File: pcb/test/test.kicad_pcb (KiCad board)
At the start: 2 copper layers, 27 parts, among them IC1 ADG904BRUZ-REEL7, J1 CONSMA013.062-G, J3 Conn_01x04, U2 TL081

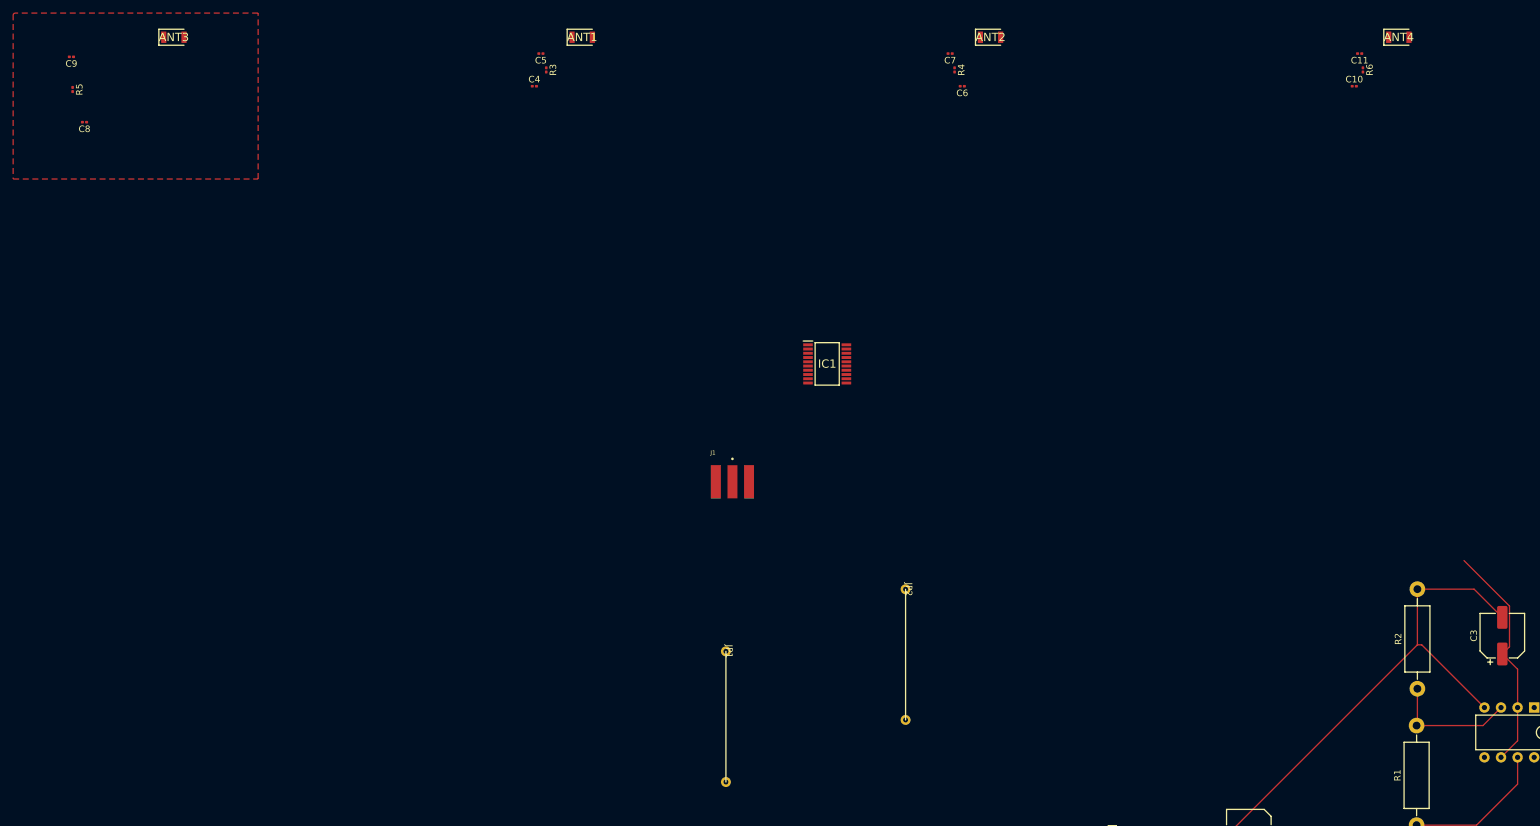
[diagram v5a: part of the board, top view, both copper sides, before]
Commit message: routage guides d'onde
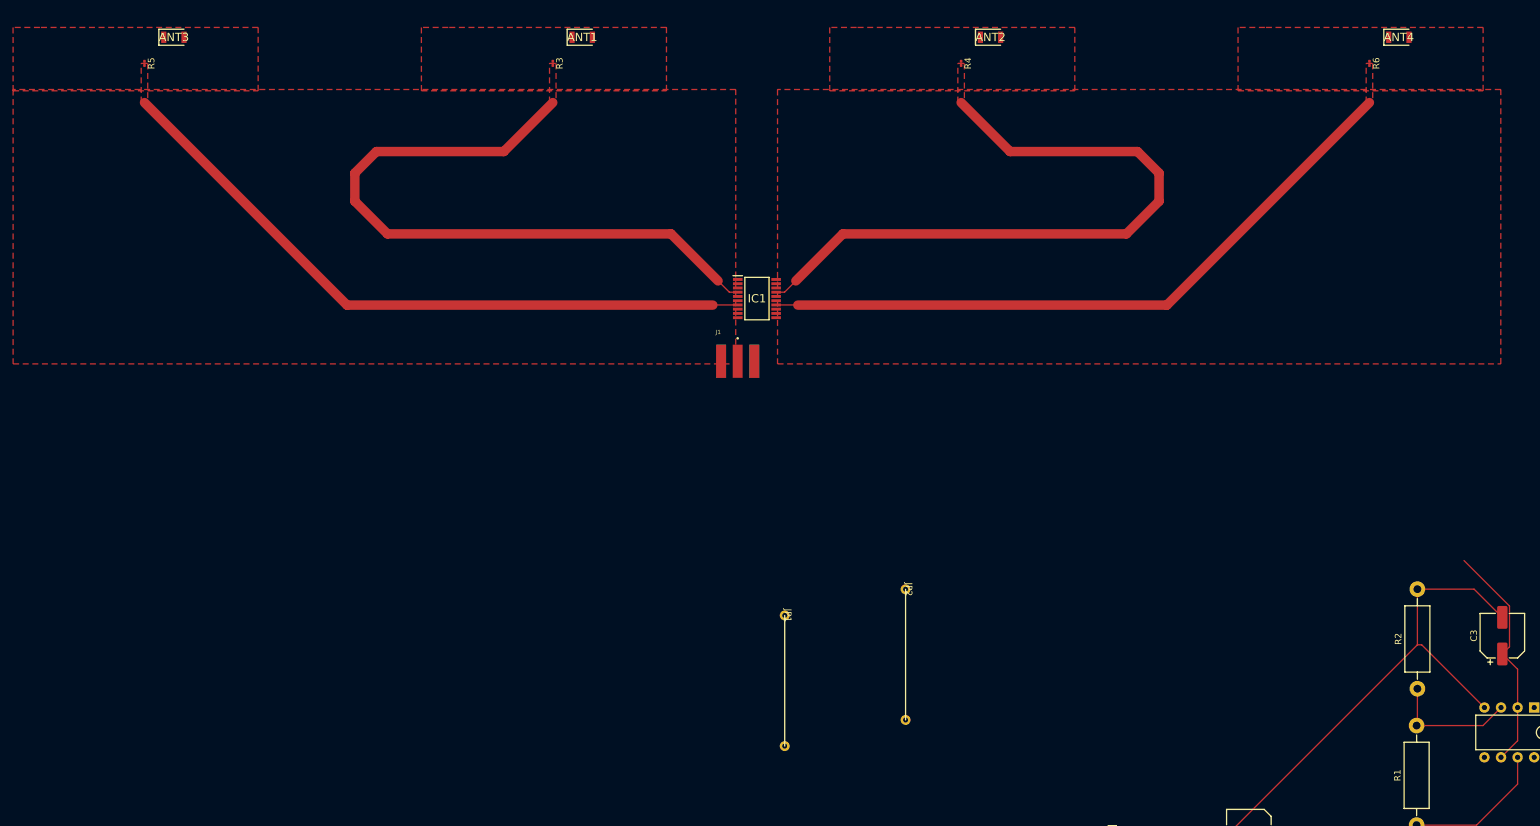
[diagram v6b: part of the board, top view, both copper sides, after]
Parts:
- removed C10, C11, C4, C5, C6, C7, C8, C9: C, Capacitor_SMD:C_0201_0603Metric
- moved J1 18.5 mm to (136.3, 102.1)
- moved IC1 14.7 mm to (139.2, 90.0)
- moved R5 11.7 mm to (45.5, 54.0)
- moved JP1 10.5 mm to (143.5, 138.5)
- moved R3 1.41 mm to (108.0, 54.0)
- moved R4 1.41 mm to (170.5, 54.0)
- moved R6 1.41 mm to (233.0, 54.0)
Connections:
- ANT1 pad 1: Net-(ANT1-FEED) -> GND
- ANT2 pad 1: Net-(ANT2-FEED) -> GND
- ANT3 pad 1: Net-(ANT3-FEED) -> GND
- ANT4 pad 1: Net-(ANT4-FEED) -> GND
- R3 pad 1: Net-(ANT1-FEED) -> GND
- R4 pad 1: Net-(ANT2-FEED) -> GND
- R5 pad 1: Net-(ANT3-FEED) -> GND
- R6 pad 1: Net-(ANT4-FEED) -> GND
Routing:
- net Net-(IC1-RF4): track 0.00 -> 103.7 mm
- net Net-(IC1-RF3): track 0.00 -> 103.7 mm
- net Net-(IC1-RF2): track 0.00 -> 103.5 mm
- net Net-(IC1-RF1): track 0.00 -> 103.5 mm
- added copper zone on F.Cu, net Net-(IC1-RF1)
- added copper zone on F.Cu, net Net-(IC1-RF2)
- added copper zone on F.Cu, net Net-(IC1-RF3)
- added copper zone on F.Cu, net Net-(IC1-RF4)

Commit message: aaaaaaaah
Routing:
- net Net-(IC1-RFC): track 0.00 -> 6.68 mm
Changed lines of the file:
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@@
 			)
 		)
+		(model "C:/Users/paulj/Documents/projet_peripheral/components/ST0147-00-011-A/3D/ST0147-00-011-A.stp"
+			(offset
+				(xyz 0 0 0)
+			)
+			(scale
+				(xyz 1 1 1)
+			)
+			(rotate
+				(xyz 0 0 0)
+			)
+		)
 	)
 	(footprint "test_footprint_library:ANTC3016X55N"
@@
 			)
 		)
+		(model "C:/Users/paulj/Documents/projet_peripheral/components/ST0147-00-011-A/3D/ST0147-00-011-A.stp"
+			(offset
+				(xyz 0 0 0)
+			)
+			(scale
+				(xyz 1 1 1)
+			)
+			(rotate
+				(xyz 0 0 0)
+			)
+		)
 	)
 	(footprint "Resistor_SMD:R_0201_0603Metric"
@@
 			)
 		)
+		(model "C:/Users/paulj/Documents/projet_peripheral/components/ST0147-00-011-A/3D/ST0147-00-011-A.stp"
+			(offset
+				(xyz 0 0 0)
+			)
+			(scale
+				(xyz 1 1 1)
+			)
+			(rotate
+				(xyz 0 0 0)
+			)
+		)
 	)
 	(footprint "Resistor_THT:R_Axial_DIN0411_L9.9mm_D3.6mm_P15.24mm_Horizontal"
@@
 			)
 		)
+		(model "C:/Users/paulj/Documents/projet_peripheral/components/ADG904BRUZ-REEL7/3D/ADG904BRUZ-REEL7.stp"
+			(offset
+				(xyz 0 0 0)
+			)
+			(scale
+				(xyz 1 1 1)
+			)
+			(rotate
+				(xyz 0 0 0)
+			)
+		)
 	)
 	(footprint "test_footprint_library:LINX_CONSMA013.062-G"
@@
 			)
 		)
+		(model "C:/Users/paulj/Documents/projet_peripheral/components/ST0147-00-011-A/3D/ST0147-00-011-A.stp"
+			(offset
+				(xyz 0 0 0)
+			)
+			(scale
+				(xyz 1 1 1)
+			)
+			(rotate
+				(xyz 0 0 0)
+			)
+		)
 	)
 	(footprint "Package_DIP:DIP-8_W7.62mm"
@@
 	)
 	(segment
+		(start 136.3 92.937)
+		(end 136.312 92.925)
+		(width 0.2)
+		(layer "F.Cu")
+		(net 6)
+	)
+	(segment
+		(start 136.3 99.5975)
+		(end 136.3 92.937)
+		(width 0.2)
+		(layer "F.Cu")
+		(net 6)
+	)
+	(segment
 		(start 240.34 155.24)
 		(end 240.22 155.36)
@@
 		(polygon
 			(pts
-				(xy 142.4 58) (xy 142.4 100) (xy 253.106751 100) (xy 253.106751 100) (xy 253.106751 58)
+				(xy 142.4 58) (xy 142.4 100) (xy 253.106751 100) (xy 253.106751 58)
 			)
 		)
@@
 		(polygon
 			(pts
-				(xy 25.393249 58) (xy 25.393249 100) (xy 136 100) (xy 136 100) (xy 136 58) (xy 25.393249 58)
+				(xy 25.393249 58) (xy 25.393249 100) (xy 136 100) (xy 136 58)
 			)
 		)

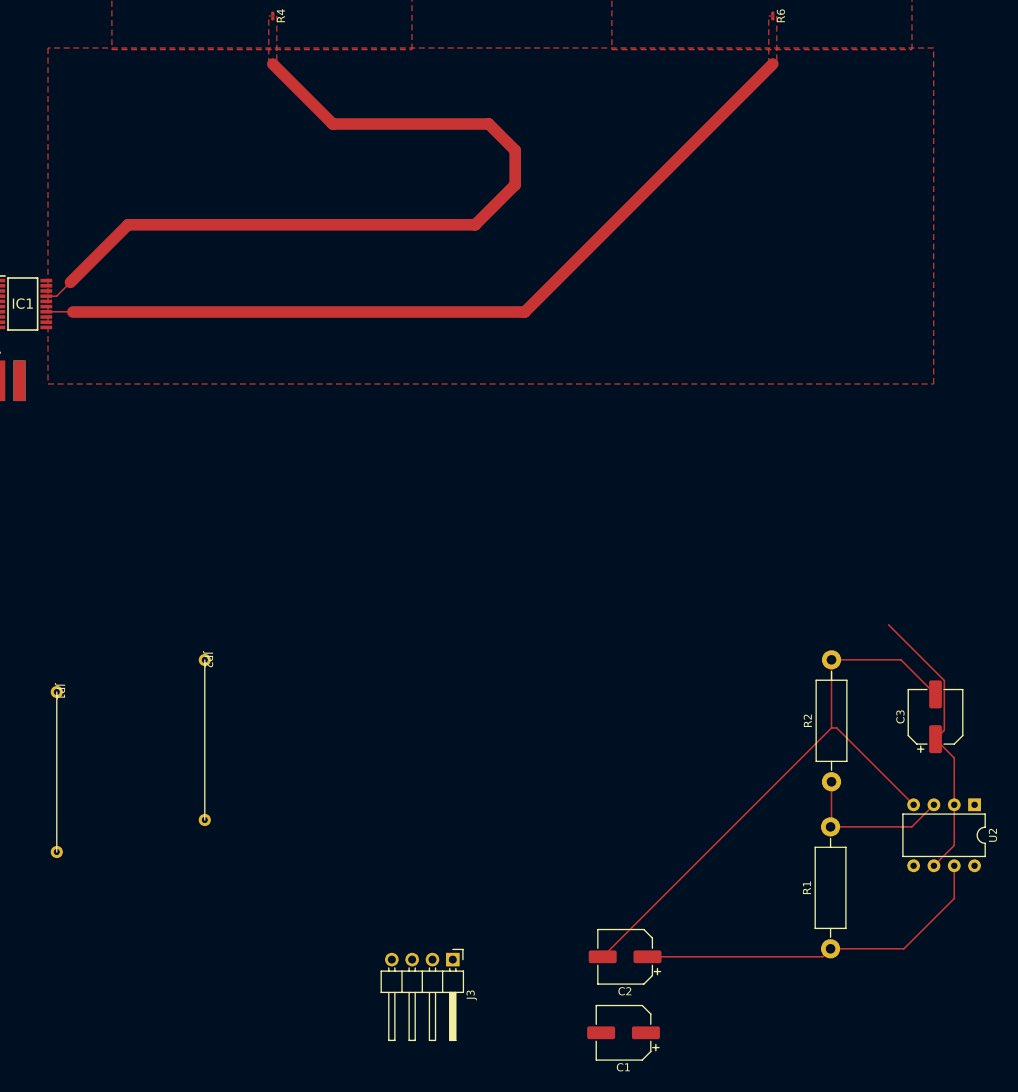
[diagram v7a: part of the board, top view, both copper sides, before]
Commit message: composants pour 2V5 placés
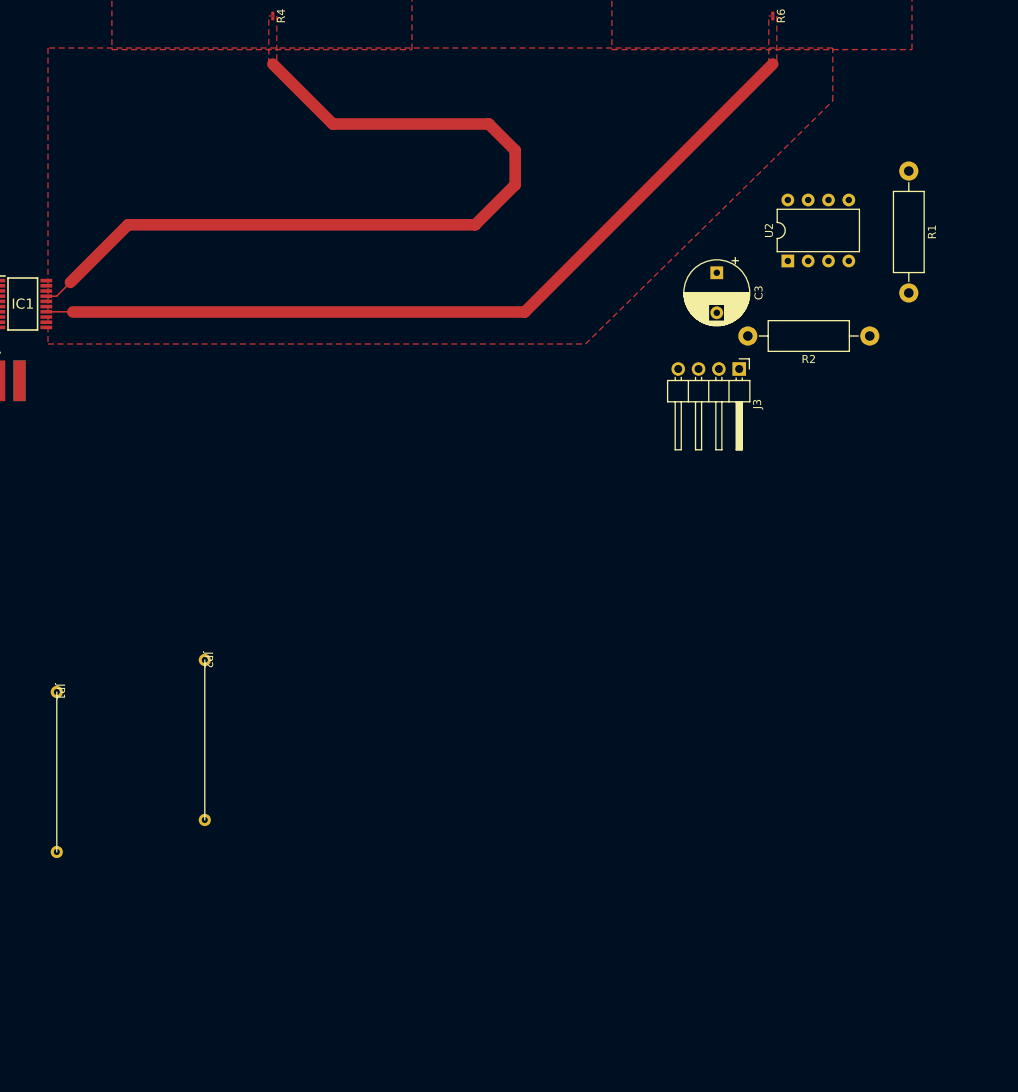
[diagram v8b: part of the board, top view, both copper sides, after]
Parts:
- removed C1: C, Capacitor_SMD:CP_Elec_6.3x5.4
- removed C2: C_Polarized, Capacitor_SMD:CP_Elec_6.3x5.4
- C3: footprint Capacitor_SMD:CP_Elec_6.3x5.4 -> Capacitor_THT:CP_Radial_D8.0mm_P5.00mm
- moved R1 97.7 mm to (250.0, 73.4), turned to -90 degrees
- moved J3 82.0 mm to (228.8, 98.1)
- moved U2 71.9 mm to (234.9, 84.6), turned to 90 degrees
- moved C3 61.9 mm to (226.0, 86.1), turned to -90 degrees
- moved R2 55.9 mm to (245.1, 94.0), turned to 180 degrees
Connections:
- ANT1 pad 2: GND -> unconnected-(ANT1-NC-Pad2)
- ANT2 pad 2: GND -> unconnected-(ANT2-NC-Pad2)
- ANT3 pad 2: GND -> unconnected-(ANT3-NC-Pad2)
- ANT4 pad 2: GND -> unconnected-(ANT4-NC-Pad2)
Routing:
- net GND: track 78.8 -> 0.00 mm
- net +5V: track 45.9 -> 0.00 mm
- net +2V5: track 35.5 -> 0.00 mm
- net Net-(U2-+): track 19.8 -> 0.00 mm
